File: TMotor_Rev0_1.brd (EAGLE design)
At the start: 91.5 x 74.3 mm, 78 parts, among them J1 5015680507, J10 5015680207, J2 5015680507, J7 5015680207, J8 5015680207, J9 5015680207, U1 INA125U, U2 INA125U, U3 INA125U, U4 INA125U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

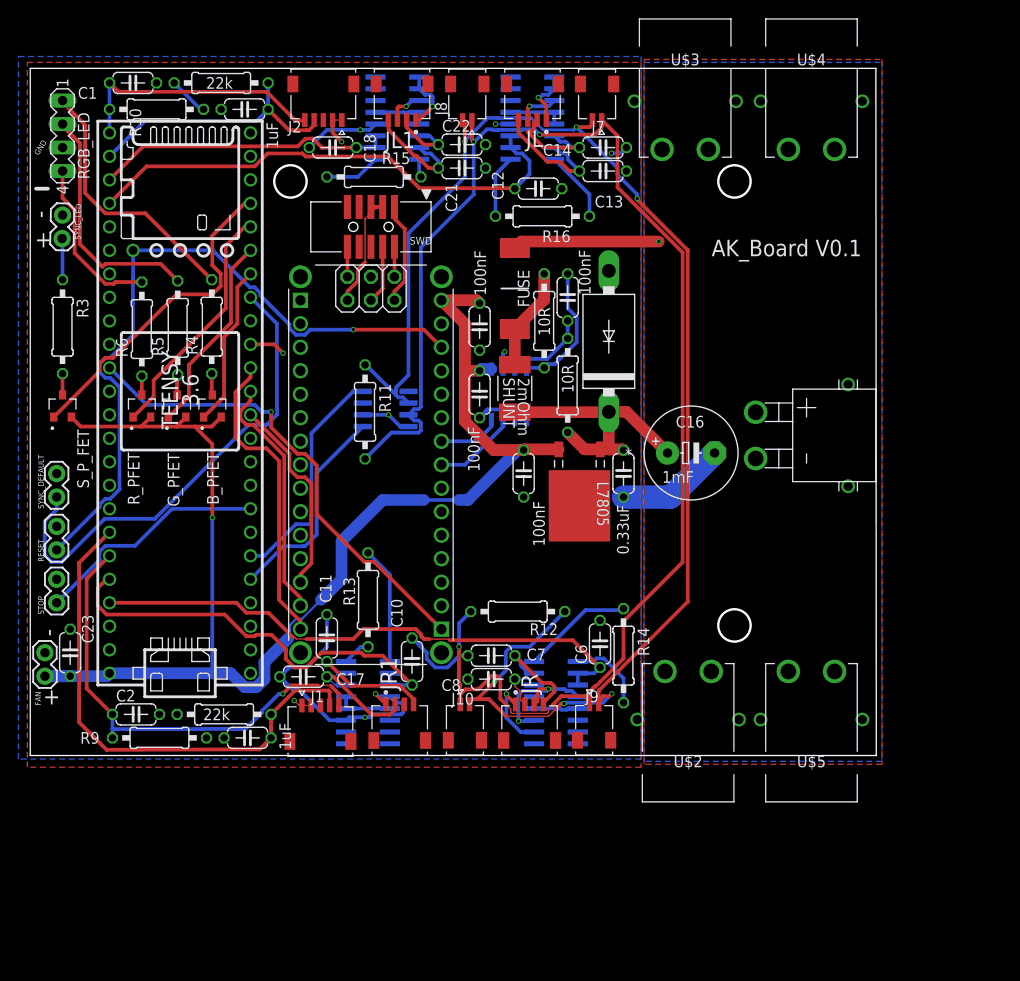
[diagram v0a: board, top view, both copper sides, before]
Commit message: cross connected the spi coms pins due to TSPISlave function
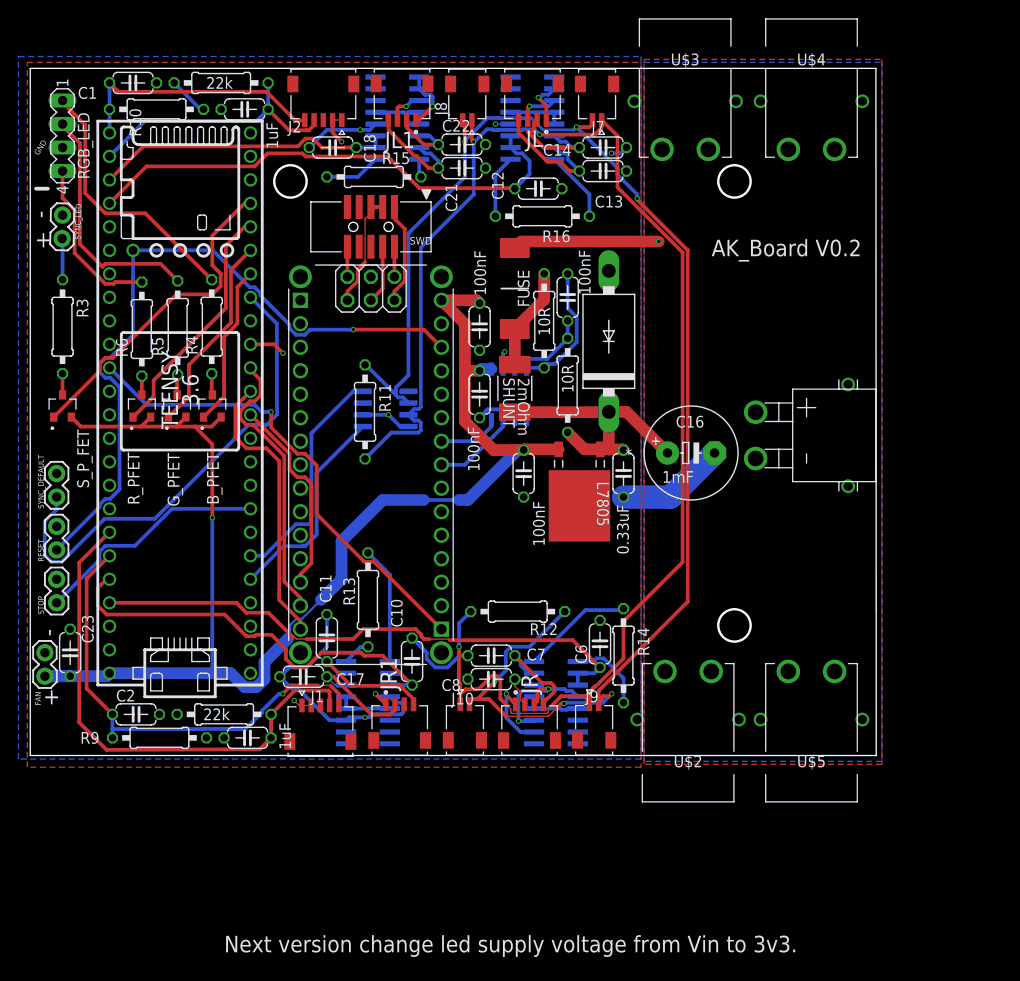
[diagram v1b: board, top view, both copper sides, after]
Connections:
- net MISO: now also U$1.11/MOSI; no longer U$1.12/MISO
- net MOSI: now also U$1.12/MISO; no longer U$1.11/MOSI
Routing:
- net MOSI: track 26.7 -> 30.5 mm
- net MISO: track 33.1 -> 30.6 mm
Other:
- board text added: "AK_Board V0.2"
- board text added: "Next version change led supply voltage from Vin to 3v3."
- board text removed: "AK_Board V0.1"
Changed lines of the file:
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@@
 <layer number="20" name="Dimension" color="24" fill="1" visible="yes" active="yes"/>
 <layer number="21" name="tPlace" color="7" fill="1" visible="yes" active="yes"/>
-<layer number="22" name="bPlace" color="7" fill="1" visible="no" active="yes"/>
+<layer number="22" name="bPlace" color="7" fill="1" visible="yes" active="yes"/>
 <layer number="23" name="tOrigins" color="15" fill="1" visible="yes" active="yes"/>
 <layer number="24" name="bOrigins" color="15" fill="1" visible="yes" active="yes"/>
@@
 <circle x="42.475" y="69.365" radius="1.75" width="0.254" layer="20"/>
 <circle x="42.475" y="21.365" radius="1.75" width="0.254" layer="20"/>
-<text x="40.005" y="61.2775" size="1.778" layer="21">AK_Board V0.1</text>
+<text x="40.005" y="61.2775" size="1.778" layer="21">AK_Board V0.2</text>
 <text x="-32.258" y="12.827" size="1.778" layer="121">+</text>
 <text x="-30.861" y="20.193" size="1.778" layer="121" rot="R90">-</text>
@@
 <wire x1="-33.02" y1="68.58" x2="-31.75" y2="68.58" width="0.4064" layer="121"/>
 <text x="-31.75" y="65.405" size="1.778" layer="121" rot="R90">-</text>
+<text x="-12.7" y="-13.97" size="1.778" layer="121">Next version change led supply voltage from Vin to 3v3.</text>
 </plain>
 <attributes>
@@
 <signal name="MOSI">
 <contactref element="USB" pad="B14"/>
-<contactref element="U$1" pad="11/MOSI"/>
-<wire x1="-10.922" y1="44.57964375" x2="-10.922" y2="43.68535625" width="0.4064" layer="1"/>
+<wire x1="-10.922" y1="44.45" x2="-10.922" y2="43.68535625" width="0.4064" layer="1"/>
 <wire x1="-10.922" y1="43.68535625" x2="-10.28964375" y2="43.053" width="0.4064" layer="1"/>
 <wire x1="-10.28964375" y1="43.053" x2="-9.55326875" y2="43.053" width="0.4064" layer="1"/>
-<wire x1="-9.8425" y1="46.6725" x2="-9.8425" y2="45.65914375" width="0.4064" layer="1"/>
-<wire x1="-9.8425" y1="45.65914375" x2="-10.922" y2="44.57964375" width="0.4064" layer="1"/>
 <wire x1="-4.445" y1="24.35476875" x2="-4.445" y2="23.495" width="0.4064" layer="1"/>
 <wire x1="-6.1919" y1="39.69163125" x2="-6.1919" y2="26.10166875" width="0.4064" layer="1"/>
 <wire x1="-6.1919" y1="26.10166875" x2="-4.445" y2="24.35476875" width="0.4064" layer="1"/>
 <wire x1="-9.55326875" y1="43.053" x2="-6.1919" y2="39.69163125" width="0.4064" layer="1"/>
+<contactref element="U$1" pad="12/MISO"/>
+<wire x1="-9.8425" y1="48.9894125" x2="-9.8425" y2="49.2125" width="0.4064" layer="1"/>
+<wire x1="-8.763" y1="46.22535625" x2="-8.763" y2="47.9099125" width="0.4064" layer="1"/>
+<wire x1="-8.763" y1="47.9099125" x2="-9.8425" y2="48.9894125" width="0.4064" layer="1"/>
+<wire x1="-10.922" y1="44.45" x2="-10.922" y2="44.57964375" width="0.4064" layer="1"/>
+<wire x1="-9.39535625" y1="45.593" x2="-8.763" y2="46.22535625" width="0.4064" layer="1"/>
+<wire x1="-10.922" y1="44.57964375" x2="-9.90864375" y2="45.593" width="0.4064" layer="1"/>
+<wire x1="-9.90864375" y1="45.593" x2="-9.39535625" y2="45.593" width="0.4064" layer="1"/>
 </signal>
 <signal name="TRQ_AMP_L">
@@
 <signal name="MISO">
 <contactref element="USB" pad="B15"/>
-<contactref element="U$1" pad="12/MISO"/>
-<wire x1="-9.8425" y1="49.2125" x2="-9.8425" y2="48.19914375" width="0.4064" layer="1"/>
-<wire x1="-9.8425" y1="48.19914375" x2="-11.4808" y2="46.56084375" width="0.4064" layer="1"/>
 <wire x1="-10.28964375" y1="40.513" x2="-8.128" y2="40.513" width="0.4064" layer="1"/>
-<wire x1="-11.4808" y1="41.70415625" x2="-10.28964375" y2="40.513" width="0.4064" layer="1"/>
+<wire x1="-10.28964375" y1="40.513" x2="-11.4808" y2="41.70415625" width="0.4064" layer="1"/>
 <wire x1="-4.445" y1="21.81476875" x2="-4.445" y2="20.955" width="0.4064" layer="1"/>
 <wire x1="-6.7507" y1="39.1357" x2="-6.7507" y2="24.12046875" width="0.4064" layer="1"/>
 <wire x1="-6.7507" y1="24.12046875" x2="-4.445" y2="21.81476875" width="0.4064" layer="1"/>
-<wire x1="-11.4808" y1="46.56084375" x2="-11.4808" y2="41.70415625" width="0.4064" layer="1"/>
 <wire x1="-8.128" y1="40.513" x2="-6.7507" y2="39.1357" width="0.4064" layer="1"/>
+<contactref element="U$1" pad="11/MOSI"/>
+<wire x1="-11.4808" y1="41.70415625" x2="-11.4808" y2="45.0342" width="0.4064" layer="1"/>
+<wire x1="-11.4808" y1="45.0342" x2="-9.8425" y2="46.6725" width="0.4064" layer="1"/>
 </signal>
 <signal name="SCK">
